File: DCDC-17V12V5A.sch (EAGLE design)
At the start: 38 parts, among them Q10 NMOSFET, Q9 NMOSFET, U1 LM3150MHX/NOPB

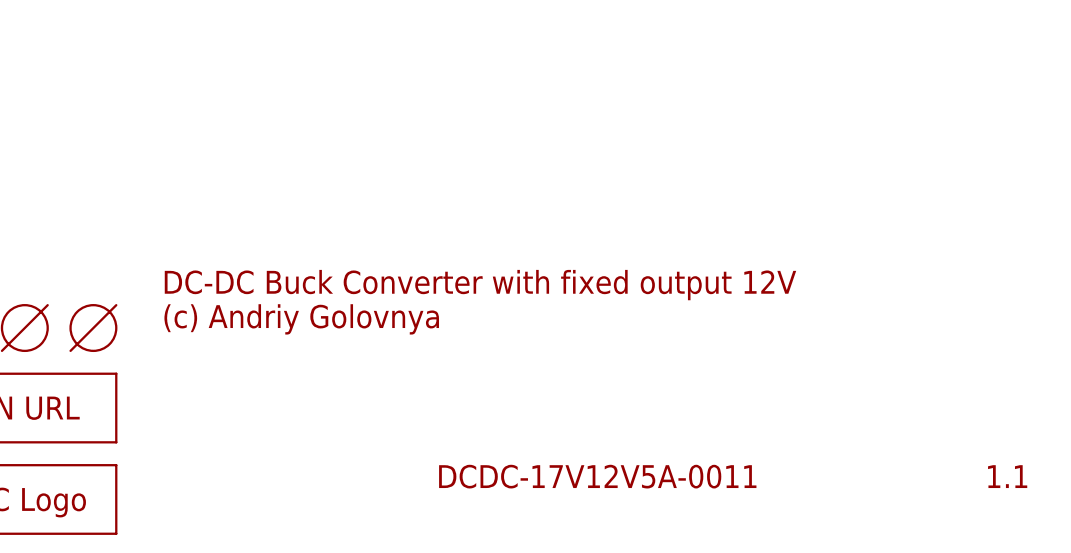
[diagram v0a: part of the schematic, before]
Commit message: Fixed typo. Generated PDF schematics.
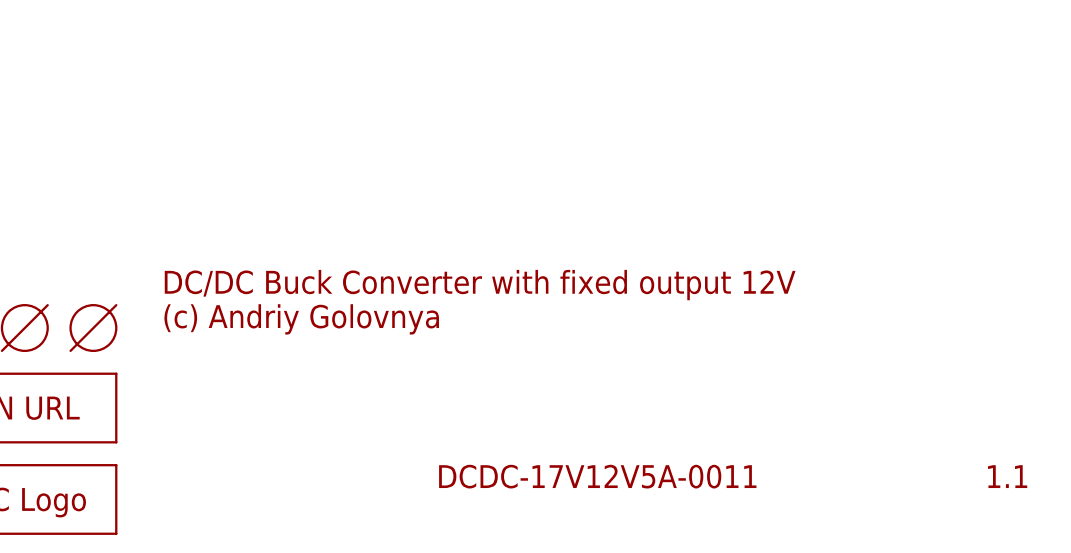
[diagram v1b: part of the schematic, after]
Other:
- note added: "DC/DC Buck Converter with fixed output 12V (c) Andriy Golovnya"
- note removed: "DC-DC Buck Converter with fixed output 12V (c) Andriy Golovnya"
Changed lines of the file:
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@@
 <text x="256.54" y="7.62" size="2.54" layer="94">1.1</text>
 <text x="195.58" y="7.62" size="2.54" layer="94">DCDC-17V12V5A-0011</text>
-<text x="165.1" y="25.4" size="2.54" layer="94">DC-DC Buck Converter with fixed output 12V
+<text x="165.1" y="25.4" size="2.54" layer="94">DC/DC Buck Converter with fixed output 12V
 (c) Andriy Golovnya</text>
 <text x="106.68" y="137.16" size="2.54" layer="94">17V to 12V Conversion</text>
